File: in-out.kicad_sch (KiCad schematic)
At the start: 21 parts, among them P1 WJ500V-5.08-2P-14-00A, P2 WJ500V-5.08-2P-14-00A, P3 Faston -12V, P4 Faston GND, P5 Faston +12V, P6 Faston +5V, U1 AMS1117-5.0

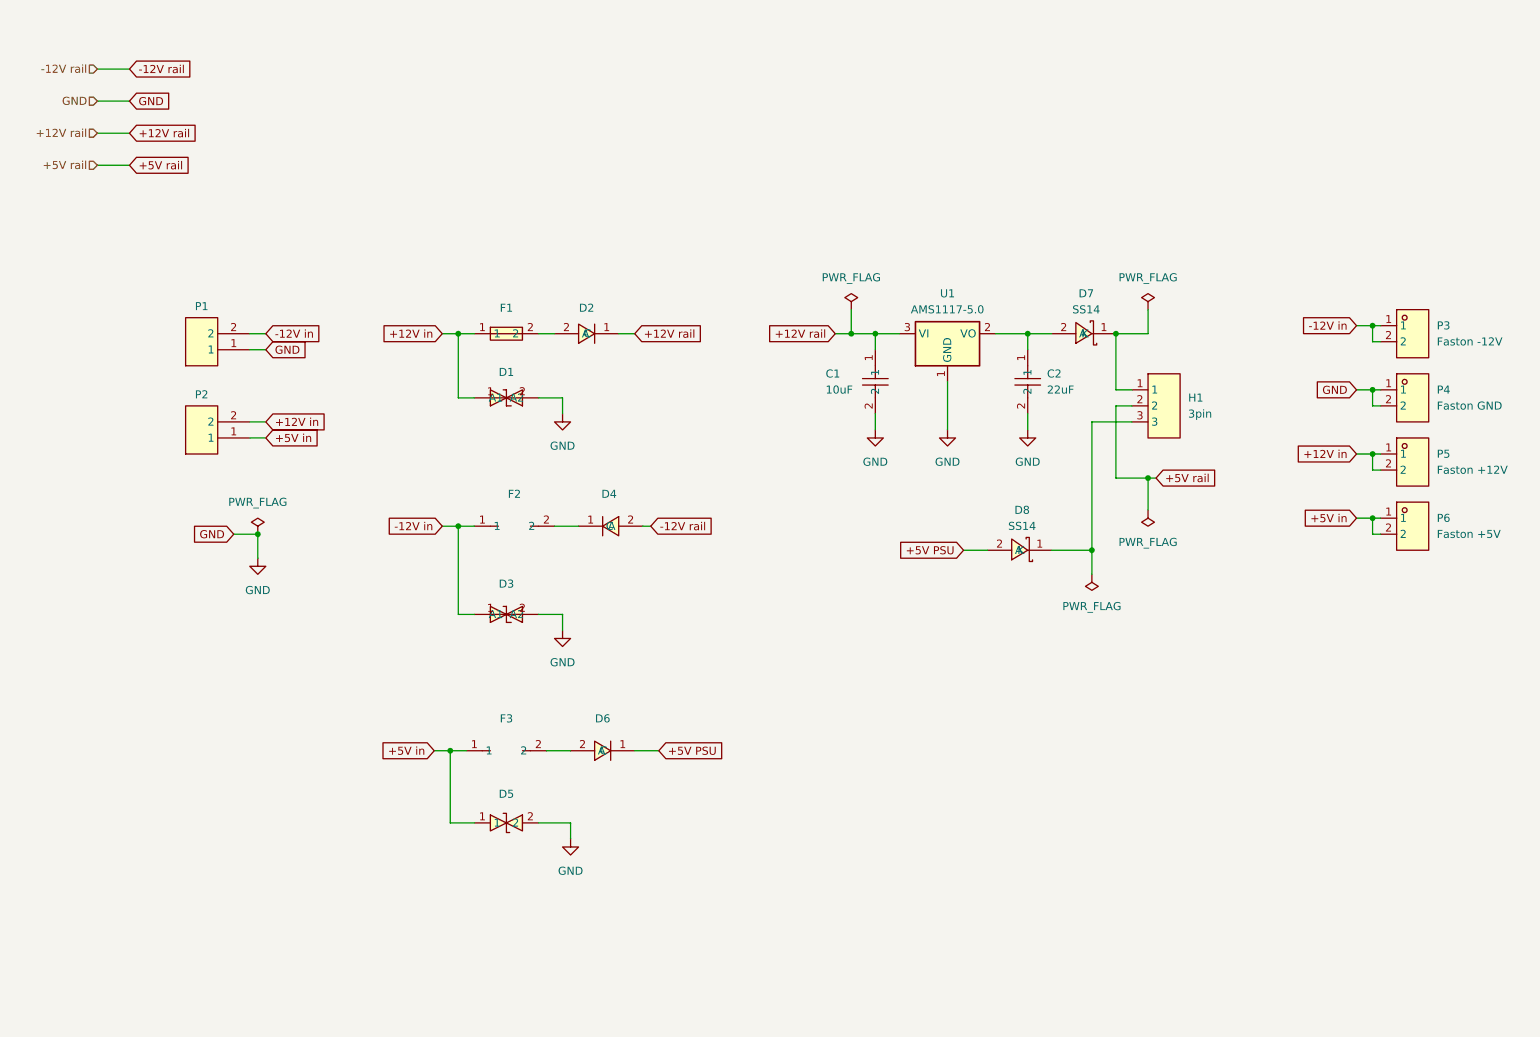
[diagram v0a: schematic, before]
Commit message: Update schematic with LED circuit and symbol library
Schematic changes (in-out.kicad_sch):
- Add LED status circuit (LED1-LED3 with R1-R3)
- Fix component naming (H1→JP1, U2/U3→LED2/LED3)
- Update F4 placement (after JP1 for +5V rail protection)
- Add resistor symbols for LED current limiting

Symbol library (zudo-bus.kicad_sym):
- Update to KiCad 9.0 format
- Add 1K resistor symbols (0603WAF1001T5E, 0805W8J0102T5E)
- Reorganize component symbols

Co-Authored-By: Claude Opus 4.5 <noreply@anthropic.com>
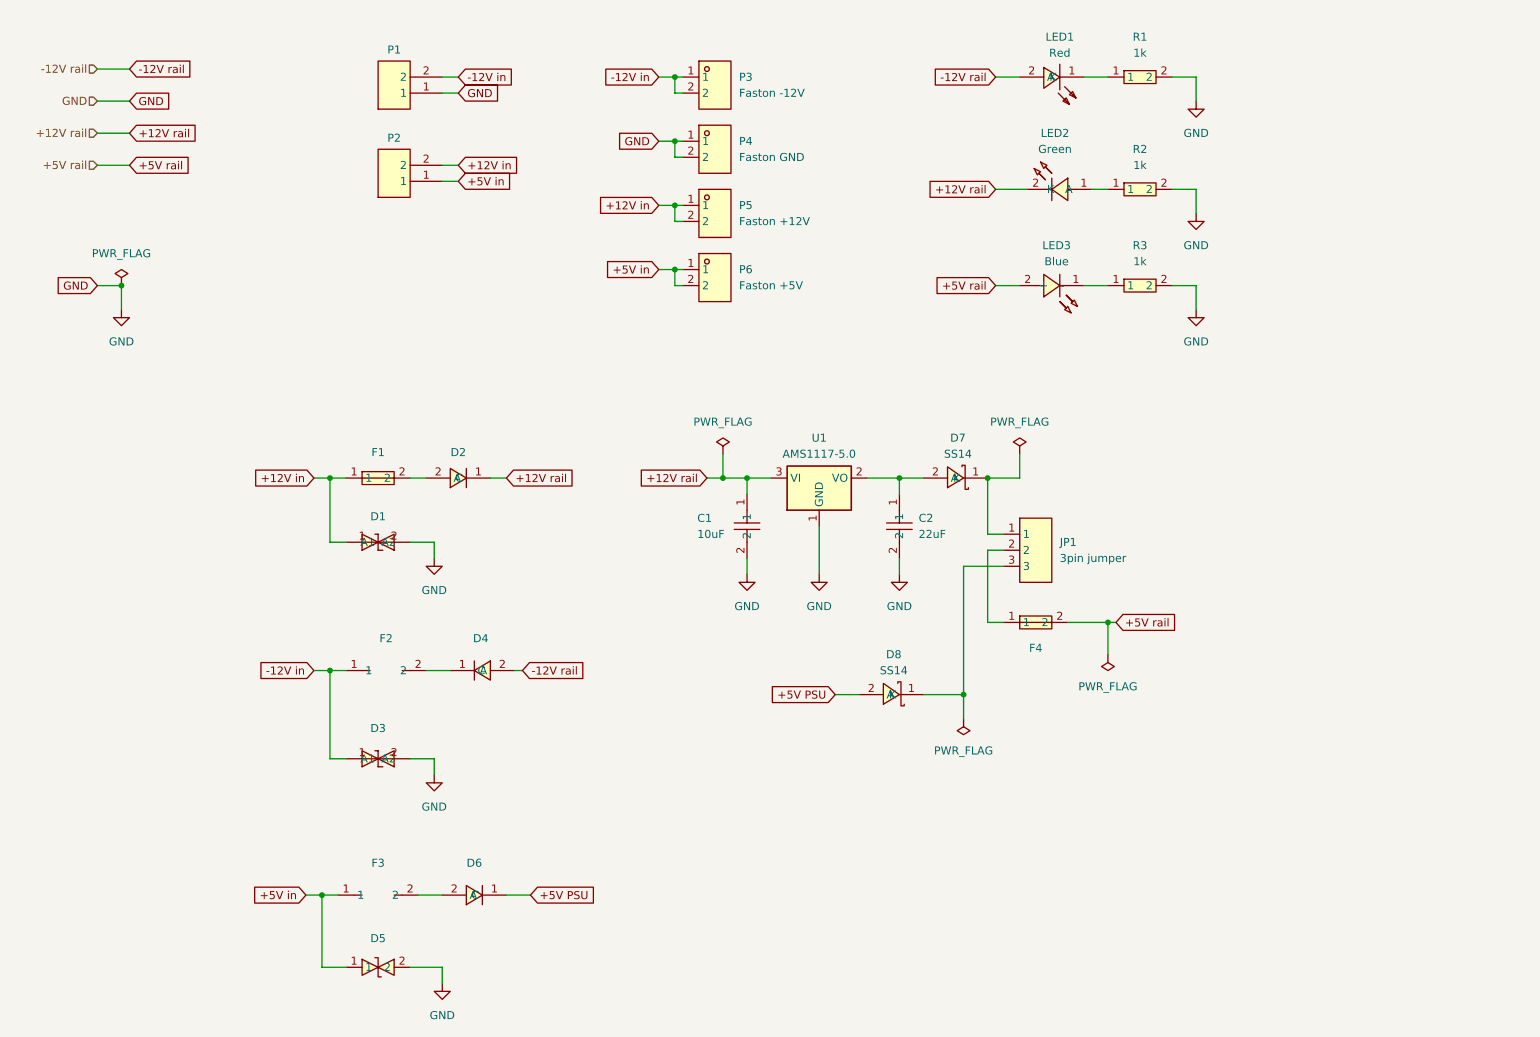
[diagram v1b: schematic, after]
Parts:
- removed H1: 3pin, easyeda2kicad:HDR-TH_3P-P2.54-V-M-1, symbol zudo-bus:Header-Male-2.54_1x3
- added F4: BSMD1812-110-33V, zudo-bus:F1812, symbol zudo-bus-new-protection:BSMD1812-110-33V
- added JP1: 3pin jumper, easyeda2kicad:HDR-TH_3P-P2.54-V-M-1, symbol zudo-bus:Header-Male-2.54_1x3
- added LED1: Red, easyeda2kicad:LED0603-RD, symbol zudo-bus:KT-0603R
- added LED2: Green, easyeda2kicad:LED0603-FD, symbol zudo-bus:YLED0603YG
- added LED3: Blue, easyeda2kicad:LED0603-RD, symbol zudo-bus:NCD1608A1
- added R1, R2, R3: 1k, easyeda2kicad:R0805, symbol zudo-bus:0805W8J0102T5E
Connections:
- net +12V rail: now also LED2.2 (K)
- net +5V rail: now also F4.2, LED3.2 (+)
- net -12V rail: now also LED1.2 (A)
- net GND: now also R1.2, R2.2, R3.2
- net at D7.1 (K): now also JP1.1
- net at D8.1 (K): now also JP1.3
- new net: LED2.1 (A), R2.1
- new net: F4.1, JP1.2
- new net: LED3.1 (-), R3.1
- new net: LED1.1 (K), R1.1
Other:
- moved on the sheet: C1, C2, D1, D2, D3, D4, D5, D6, D7, D8, F1, F2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

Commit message: Add test points (TP1-TP6) to schematic and documentation
Schematic test points added for debugging and verification:
- TP1: +12V rail (after D2)
- TP2: -12V rail (after D4)
- TP3: +5V PSU input (after D6, before D8)
- TP4: LDO +5V output (U1 output, before D7)
- TP5: +5V rail (JP1 pin 2, before F4)
- TP6: GND reference

Also fixed LED1/LED2 polarity (was reverse biased).

Documentation updates:
- circuit-diagrams.mdx: Add Diagram9 for test points
- bom.md: Update test points table with correct locations

Co-Authored-By: Claude Opus 4.5 <noreply@anthropic.com>
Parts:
- added TP1: TestPoint +12V Rail, symbol Connector:TestPoint
- added TP2: TestPoint -12V Rail, symbol Connector:TestPoint
- added TP3: TestPoint +5V IN, symbol Connector:TestPoint
- added TP4: TestPoint LDO +5V, symbol Connector:TestPoint
- added TP5: TestPoint +5V Rail, symbol Connector:TestPoint
- added TP6: TestPoint GND, symbol Connector:TestPoint
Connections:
- net +12V rail: now also LED2.1 (A), TP1.1; no longer LED2.2 (K)
- net +5V PSU: now also TP3.1
- net -12V rail: now also LED1.1 (K), TP2.1; no longer LED1.2 (A)
- net GND: now also TP6.1
- net at R2.1: now also LED2.2 (K); no longer LED2.1 (A)
- net at F4.1, JP1.2: now also TP5.1
- net at C2.1, D7.2 (A), U1.2 (VO): now also TP4.1
- net at R1.1: now also LED1.2 (A); no longer LED1.1 (K)
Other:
- moved on the sheet: F4, LED1, LED2

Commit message: Add 3D models and fix footprint paths for KiCad 3D viewer
- Add 51 3D models (.wrl/.step) to footprints/3dshapes/
- Update all footprint files to use ${KIPRJMOD}/footprints/3dshapes/
- Add fp-lib-table to map library names to project footprints
- Fix broken footprint paths in schematic (zudo-bus:F1812, etc.)
- Add TestPoint footprints to TP1-TP6 in schematic
- Update .gitignore to exclude report.txt

Co-Authored-By: Claude <noreply@anthropic.com>
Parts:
- D5: footprint :SOD-123_L2.8-W1.8-LS3.7-BI -> zudo-bus:SOD-123FL_L2.8-W1.8-LS3.7-BI
- F1, F2, F3: footprint :F1812 -> zudo-bus:F1812
- TP1, TP2, TP3, TP4, TP5, TP6: footprint (none) -> TestPoint:TestPoint_Pad_D1.5mm
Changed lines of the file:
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@@
 			)
 		)
-		(property "Footprint" ""
+		(property "Footprint" "TestPoint:TestPoint_Pad_D1.5mm"
 			(at 173.99 111.76 0)
 			(effects
@@
 			)
 		)
-		(property "Footprint" ":F1812"
+		(property "Footprint" "zudo-bus:F1812"
 			(at 77.47 162.56 0)
 			(effects
@@
 			)
 		)
-		(property "Footprint" ""
+		(property "Footprint" "TestPoint:TestPoint_Pad_D1.5mm"
 			(at 40.64 58.42 0)
 			(effects
@@
 			)
 		)
-		(property "Footprint" ""
+		(property "Footprint" "TestPoint:TestPoint_Pad_D1.5mm"
 			(at 96.52 119.38 0)
 			(effects
@@
 			)
 		)
-		(property "Footprint" ""
+		(property "Footprint" "TestPoint:TestPoint_Pad_D1.5mm"
 			(at 92.71 88.9 0)
 			(effects
@@
 			)
 		)
-		(property "Footprint" ""
+		(property "Footprint" "TestPoint:TestPoint_Pad_D1.5mm"
 			(at 168.91 83.82 0)
 			(effects
@@
 			)
 		)
-		(property "Footprint" ":F1812"
+		(property "Footprint" "zudo-bus:F1812"
 			(at 78.74 127 0)
 			(effects
@@
 			)
 		)
-		(property "Footprint" ""
+		(property "Footprint" "TestPoint:TestPoint_Pad_D1.5mm"
 			(at 95.25 154.94 0)
 			(effects
@@
 			)
 		)
-		(property "Footprint" ":SOD-123_L2.8-W1.8-LS3.7-BI"
+		(property "Footprint" "zudo-bus:SOD-123FL_L2.8-W1.8-LS3.7-BI"
 			(at 78.74 173.99 0)
 			(effects
@@
 			)
 		)
-		(property "Footprint" ":F1812"
+		(property "Footprint" "zudo-bus:F1812"
 			(at 78.74 96.52 0)
 			(effects
